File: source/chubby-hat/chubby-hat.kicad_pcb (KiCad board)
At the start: 2 copper layers, 143.5 x 91.4 mm, 128 parts, among them J1 UART, J10 HUB75, J11 HUB75, J12 HUB75, J13 v7.0, J14 v8.0, J15 HUB75, J16 Conn_01x02, J17 HUB75, J18 HUB75, J19 V7.0, J2 Conn_ARM_JTAG_SWD_10, J20 V8.0, J21 HUB75, J22 HUB75, J3 Conn_ARM_JTAG_SWD_10, J4 TC2030, J5 5V, J6 5V, J7 5V, J8 5V, J9 USB_C_Receptacle_USB2.0, Q1 AO3401A, SW1 RUN, SW2 BOOT, U1 AMS1117-3.3, U2 RP2040-Zero, U3 USBLC6-2SC6, U4 P25Q40H-SSH-IT, U5 RP2040, Y1 12M

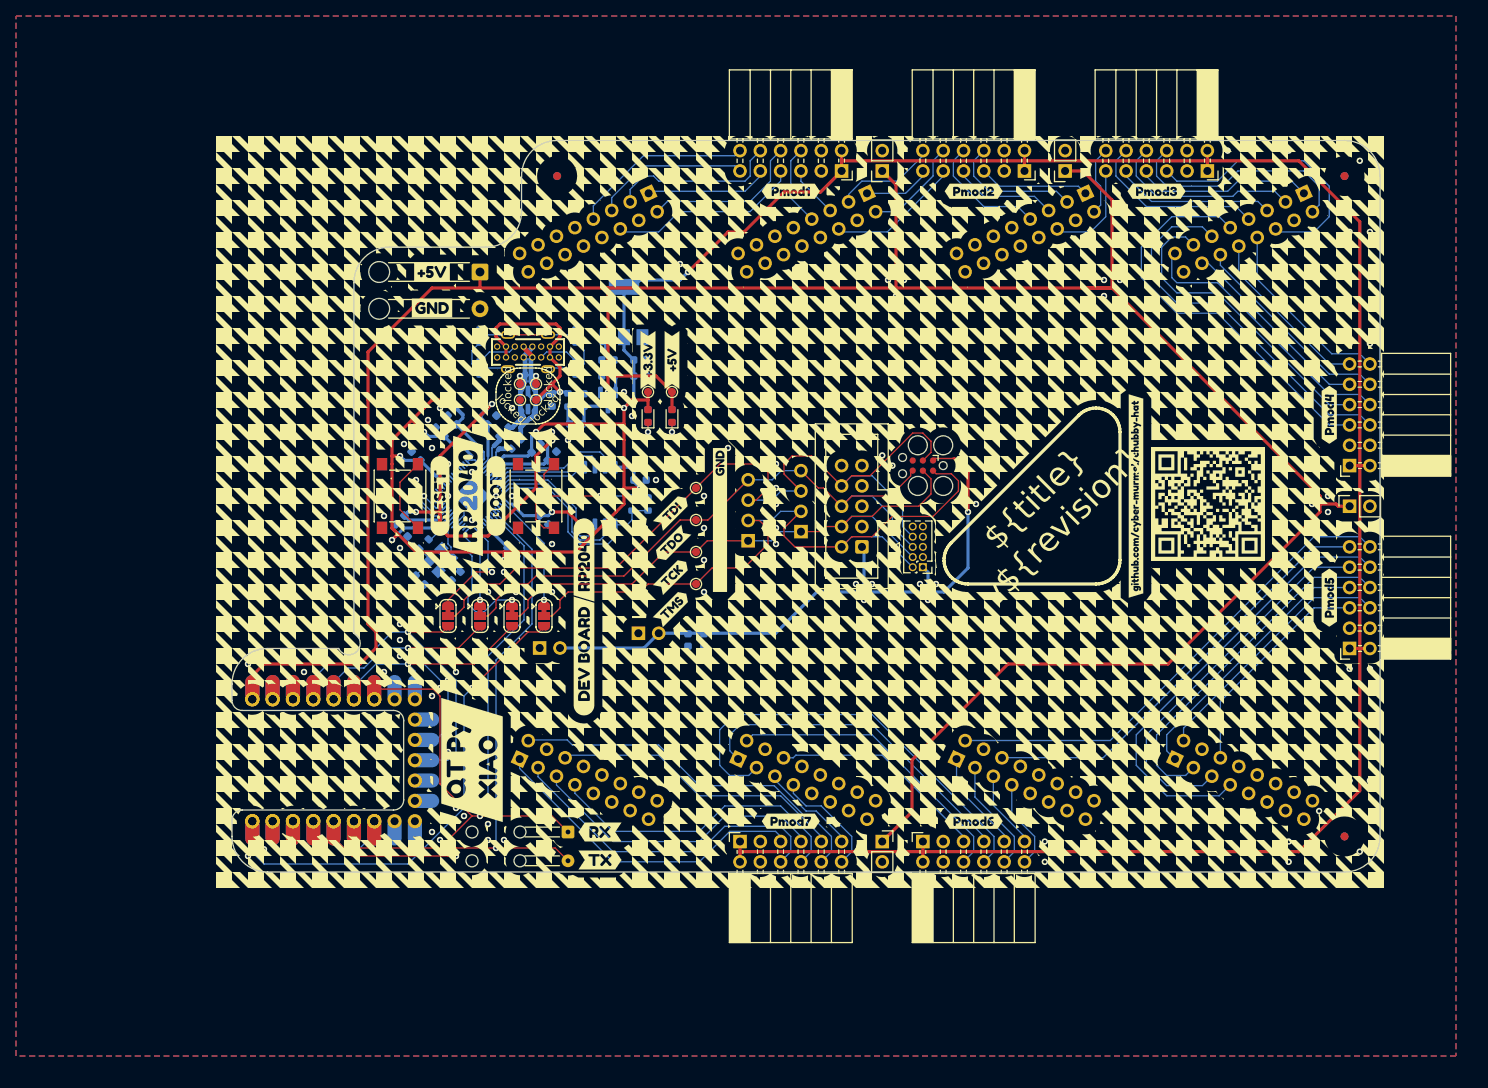
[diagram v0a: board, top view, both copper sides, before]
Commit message: add zero volt diodes to USB and modules; add status LEDs; add RP2040 SWD - closes #9
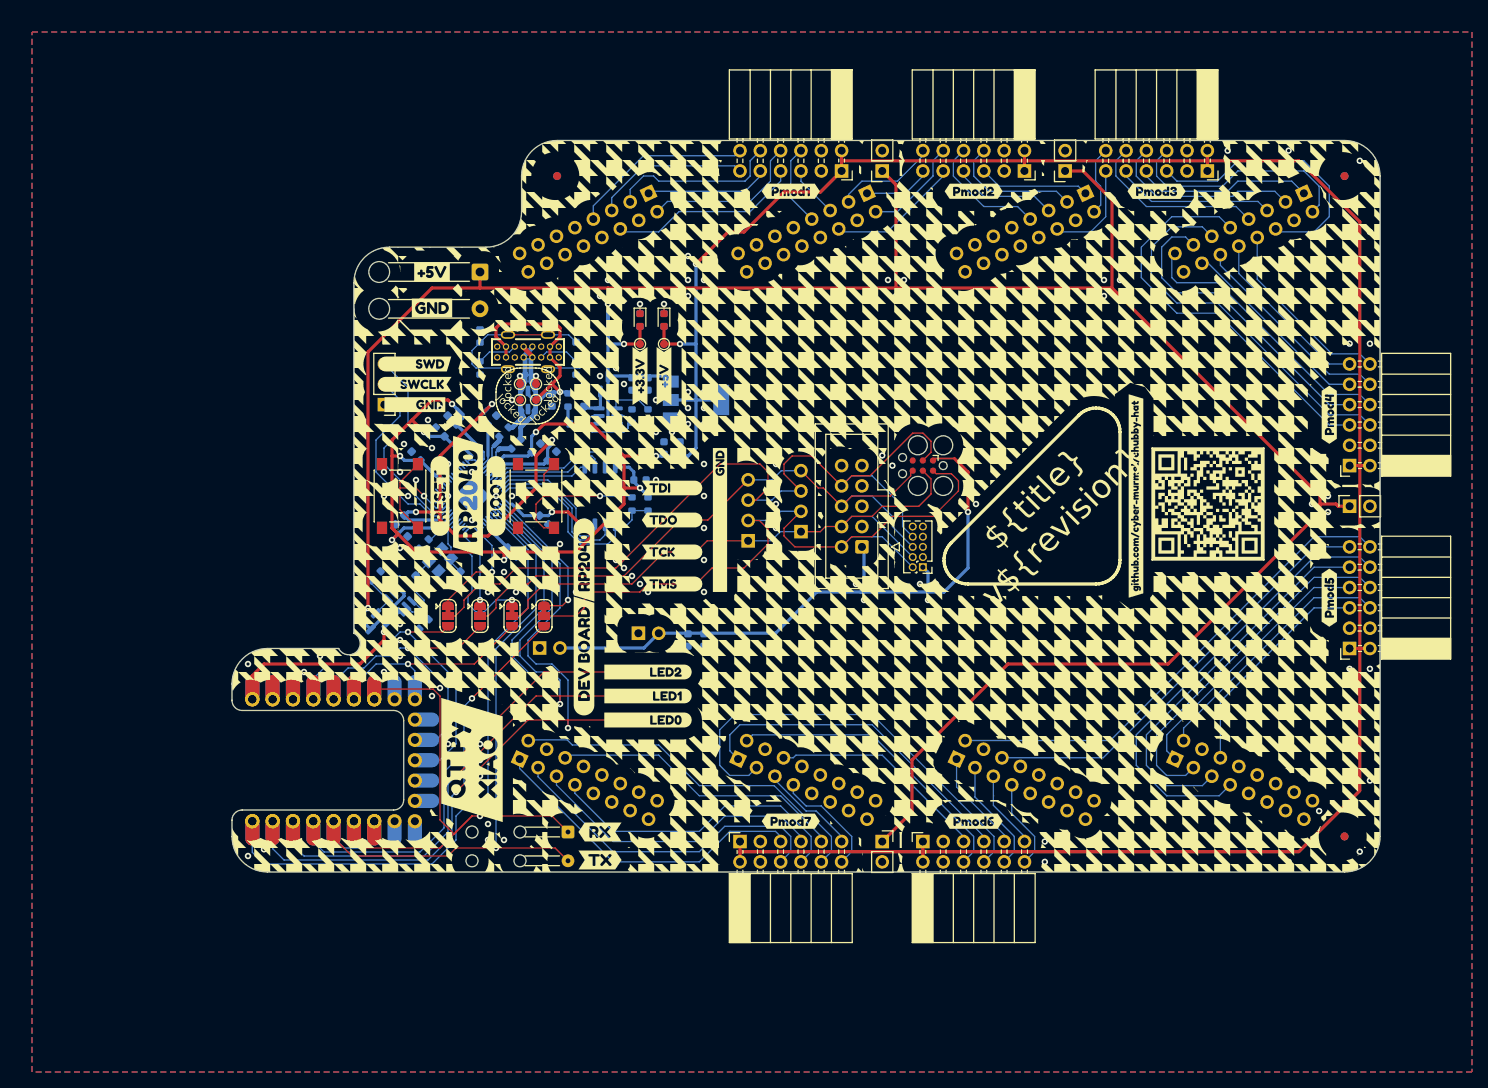
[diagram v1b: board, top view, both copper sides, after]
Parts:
- removed kibuzzard-63E54109: G***, kibuzzard-63E54109
- removed kibuzzard-63E54112: G***, kibuzzard-63E54112
- removed kibuzzard-63E5411A: G***, kibuzzard-63E5411A
- removed kibuzzard-63E54120: G***, kibuzzard-63E54120
- added D3: LED, LED_SMD:LED_0603_1608Metric, F.Cu at (175.0, 108.0)
- added D4: LED, LED_SMD:LED_0603_1608Metric, F.Cu at (175.0, 105.0)
- added D5: LED, LED_SMD:LED_0603_1608Metric, F.Cu at (175.0, 102.0)
- added J1: RP2040.SWD, Connector_PinHeader_2.54mm:PinHeader_1x03_P2.54mm_Vertical, F.Cu at (146.1, 68.6)
- added Q2: AO3401A, Package_TO_SOT_SMD:SOT-23, B.Cu at (174.0, 66.0)
- added Q3: BC807DS,115, Package_SO:SC-74-6_1.5x2.9mm_P0.95mm, B.Cu at (148.0, 93.0)
- added Q4: AO3401A, Package_TO_SOT_SMD:SOT-23, B.Cu at (145.0, 96.0)
- added R10: 47k, Resistor_SMD:R_0603_1608Metric, B.Cu at (179.0, 70.0)
- added R11: 10k, Resistor_SMD:R_0603_1608Metric, B.Cu at (151.0, 96.0)
- added R12: 47k, Resistor_SMD:R_0603_1608Metric, B.Cu at (145.0, 90.0)
- added R3: 5.1k, Resistor_SMD:R_0603_1608Metric, B.Cu at (175.0, 108.0)
- added R4: 5.1k, Resistor_SMD:R_0603_1608Metric, B.Cu at (175.0, 105.0)
- added R5: 5.1k, Resistor_SMD:R_0603_1608Metric, B.Cu at (175.0, 102.0)
- added R9: 10k, Resistor_SMD:R_0603_1608Metric, B.Cu at (177.0, 70.0)
- added kibuzzard-63E66495: G***, kibuzzard-63E66495, F.Cu at (182.0, 79.0)
- added kibuzzard-63E664A0: G***, kibuzzard-63E664A0, F.Cu at (182.0, 83.0)
- added kibuzzard-63E664C7: G***, kibuzzard-63E664C7, F.Cu at (182.0, 91.0)
- added kibuzzard-63E664D7: G***, kibuzzard-63E664D7, F.Cu at (182.0, 87.0)
- added kibuzzard-63E665A8: G***, kibuzzard-63E665A8, F.Cu at (149.9, 63.5)
- added kibuzzard-63E665B7: G***, kibuzzard-63E665B7, F.Cu at (149.9, 66.0)
- added kibuzzard-63E67724: G***, kibuzzard-63E67724, F.Cu at (149.9, 68.6)
- added kibuzzard-63E6D9D7: G***, kibuzzard-63E6D9D7, F.Cu at (179.0, 102.0)
- added kibuzzard-63E6D9E4: G***, kibuzzard-63E6D9E4, F.Cu at (179.0, 105.0)
- added kibuzzard-63E6D9E9: G***, kibuzzard-63E6D9E9, F.Cu at (179.0, 108.0)
- Q1: value AO3401A -> BC807DS,115; footprint Package_TO_SOT_SMD:SOT-23 -> Package_SO:SC-74-6_1.5x2.9mm_P0.95mm
- R1, R2: value 1k -> 5.1k
- moved U1 14.2 mm to (185.0, 68.0), turned to 0 degrees
- moved D1 12.6 mm to (178.0, 58.0), turned to -90 degrees
- moved R1 12.6 mm to (178.0, 58.0), turned to -90 degrees
- moved D2 12.2 mm to (181.0, 58.0), turned to -90 degrees
- moved R2 12.2 mm to (181.0, 58.0), turned to -90 degrees
- moved C4 12.1 mm to (183.0, 74.0), turned to -90 degrees
- moved C3 9.49 mm to (181.0, 74.0), turned to -90 degrees
- moved TP1 7.21 mm to (178.0, 61.0), turned to 180 degrees
- moved TP2 6.32 mm to (181.0, 61.0), turned to 180 degrees
- moved C1 5.83 mm to (179.0, 66.0), turned to 90 degrees
- moved C2 3.16 mm to (177.0, 66.0), turned to 90 degrees
- moved kibuzzard-63E58302 2.24 mm to (181.0, 65.0)
- moved kibuzzard-63E5830C 2.24 mm to (178.0, 65.0)
- moved Q1 2.00 mm to (174.0, 70.0), turned to 180 degrees
- renumbered C7 to C6, C6 to C7, J9 to J10, J10 to J11, J11 to J12, J12 to J13, J13 to J14, J14 to J15, J15 to J16, J16 to J17, J17 to J18, J18 to J19, J19 to J20, J20 to J21, J21 to J22, J22 to J23, J1 to J5, J5 to J6, J6 to J7, J7 to J8, J8 to J9, R6 to R13, R7 to R14, R8 to R15, R9 to R16, R10 to R17, R3 to R6, R4 to R7, R5 to R8
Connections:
- A1 pad 14: +5V -> +5V_{module}
- A1 pad 2: unconnected-(A1-Pad2) -> /RP2040/GPIO1
- A1 pad 3: unconnected-(A1-Pad3) -> /RP2040/GPIO2
- A1 pad 4: unconnected-(A1-Pad4) -> /RP2040/GPIO3
- Q1 pad 1: GND -> Net-(Q1-Pad1)
- Q1 pad 2: +5V -> Net-(Q1-Pad2)
- Q1 pad 3: /Type C USB 2.0/VBUS_FB1 -> +5V
- U2 pad 1: +5V -> +5V_{module}
- U2 pad 20: unconnected-(U2-Pad20) -> /RP2040/GPIO3
- U2 pad 21: unconnected-(U2-Pad21) -> /RP2040/GPIO2
- U2 pad 22: unconnected-(U2-Pad22) -> /RP2040/GPIO1
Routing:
- net /RP2040/GPIO1: track 0.00 -> 91.8 mm, vias 0 -> 2
- net /RP2040/GPIO2: track 0.00 -> 86.8 mm, vias 0 -> 2
- net /RP2040/GPIO3: track 0.00 -> 81.9 mm, vias 0 -> 2
- net +5V_{module}: track 0.00 -> 24.5 mm, vias 0 -> 1
- net /RP2040/SWD.SWD: track 4.43 -> 25.3 mm
- net /RP2040/SWD.SWCLK: track 4.81 -> 24.5 mm
- net Net-(Q3-Pad2): track 0.00 -> 14.3 mm
- net Net-(Q1-Pad2): track 0.00 -> 13.0 mm
- net +5V: track 341.6 -> 329.1 mm, vias 1 -> 3
- net +3V3: track 440.1 -> 449.1 mm, vias 10 -> 11
- net Net-(Q1-Pad1): track 0.00 -> 6.68 mm
- net Net-(Q3-Pad1): track 0.00 -> 5.68 mm
- net /RP2040/GPIO5: track 97.7 -> 102.6 mm
- net /RP2040/GPIO0: track 14.9 -> 18.7 mm
- net /RP2040/DVDD: track 64.4 -> 61.8 mm
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
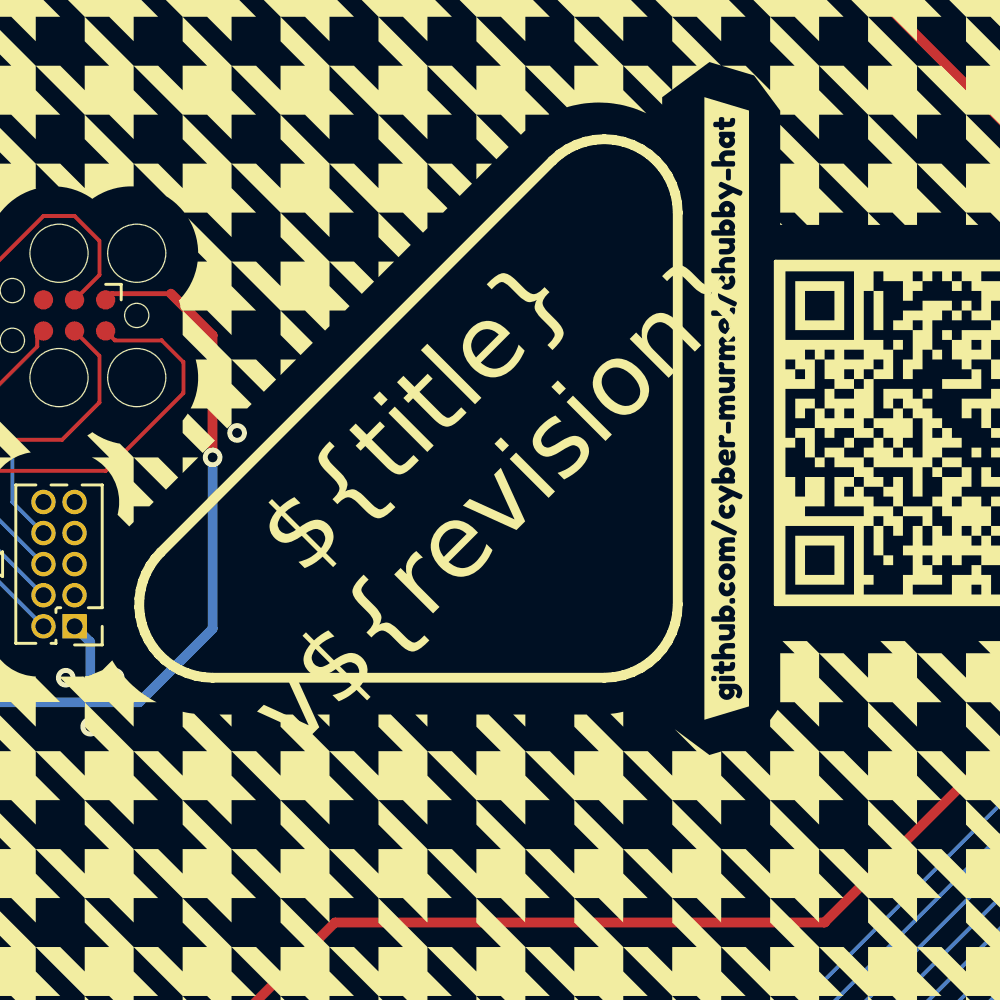
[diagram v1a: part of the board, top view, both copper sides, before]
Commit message: moved to KiCad v7.0.0
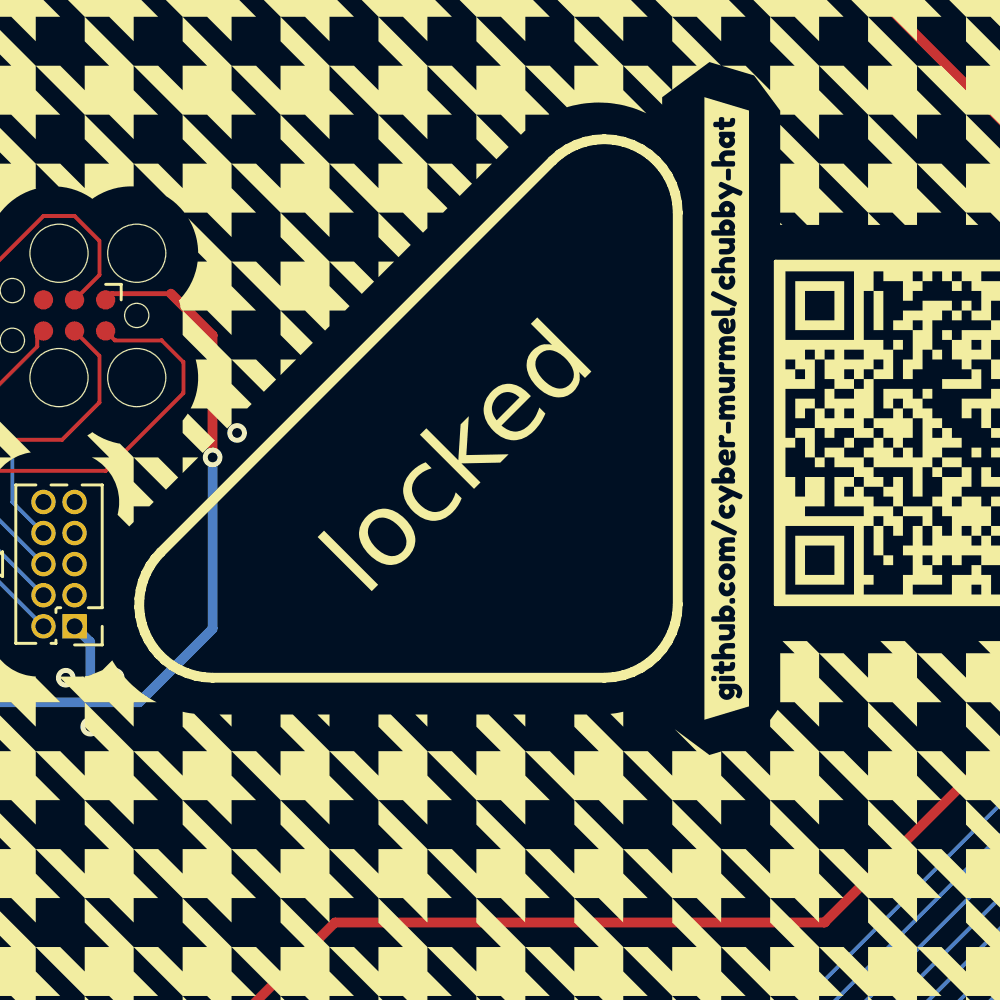
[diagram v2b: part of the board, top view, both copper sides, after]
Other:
- board text added: "locked"
- board text removed: "${title} v${revision}"
